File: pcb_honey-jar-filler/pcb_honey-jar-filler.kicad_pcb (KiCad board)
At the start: 2 copper layers, 160 x 100 mm, 88 parts, among them J1 12V, 5V, J10 OLED_3v3, GND, J11 OLED_SDA, SCL, J12 MOS out (COM, Drain), J13 230V Heater, J14 3V3, J15 12V, 5V, J16 LED2, J17 GND, J18 GND, J19 Servo, J2 12V, J20 Conn_01x07_Pin, J21 LED1, J22 Reserve, J23 Relay fallback, J24 load-cell (red, black), J25 load-cell (white, green), J26 B+ B- (free), J27 Supply, J3 3V3, J4 button1, button2, J5 4...7V, J6 Encoder A, B, J7 Encoder Button, Pos-sw, J8 MOS out (COM, Drain), K1 RT314A24, K4 RT314A24, K5 RT314A24, M1 DC-worm-gear motor (Carousell), Q1 IRLB8721PBF, Q2 IRLB8721PBF, U1 esp32-devkit-v1_30Pin, U10 LM2576T-ADJ, U3 ULN2003, U4 HX711_24-bit-ADC_weight-scale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, U9 LM2576T-5

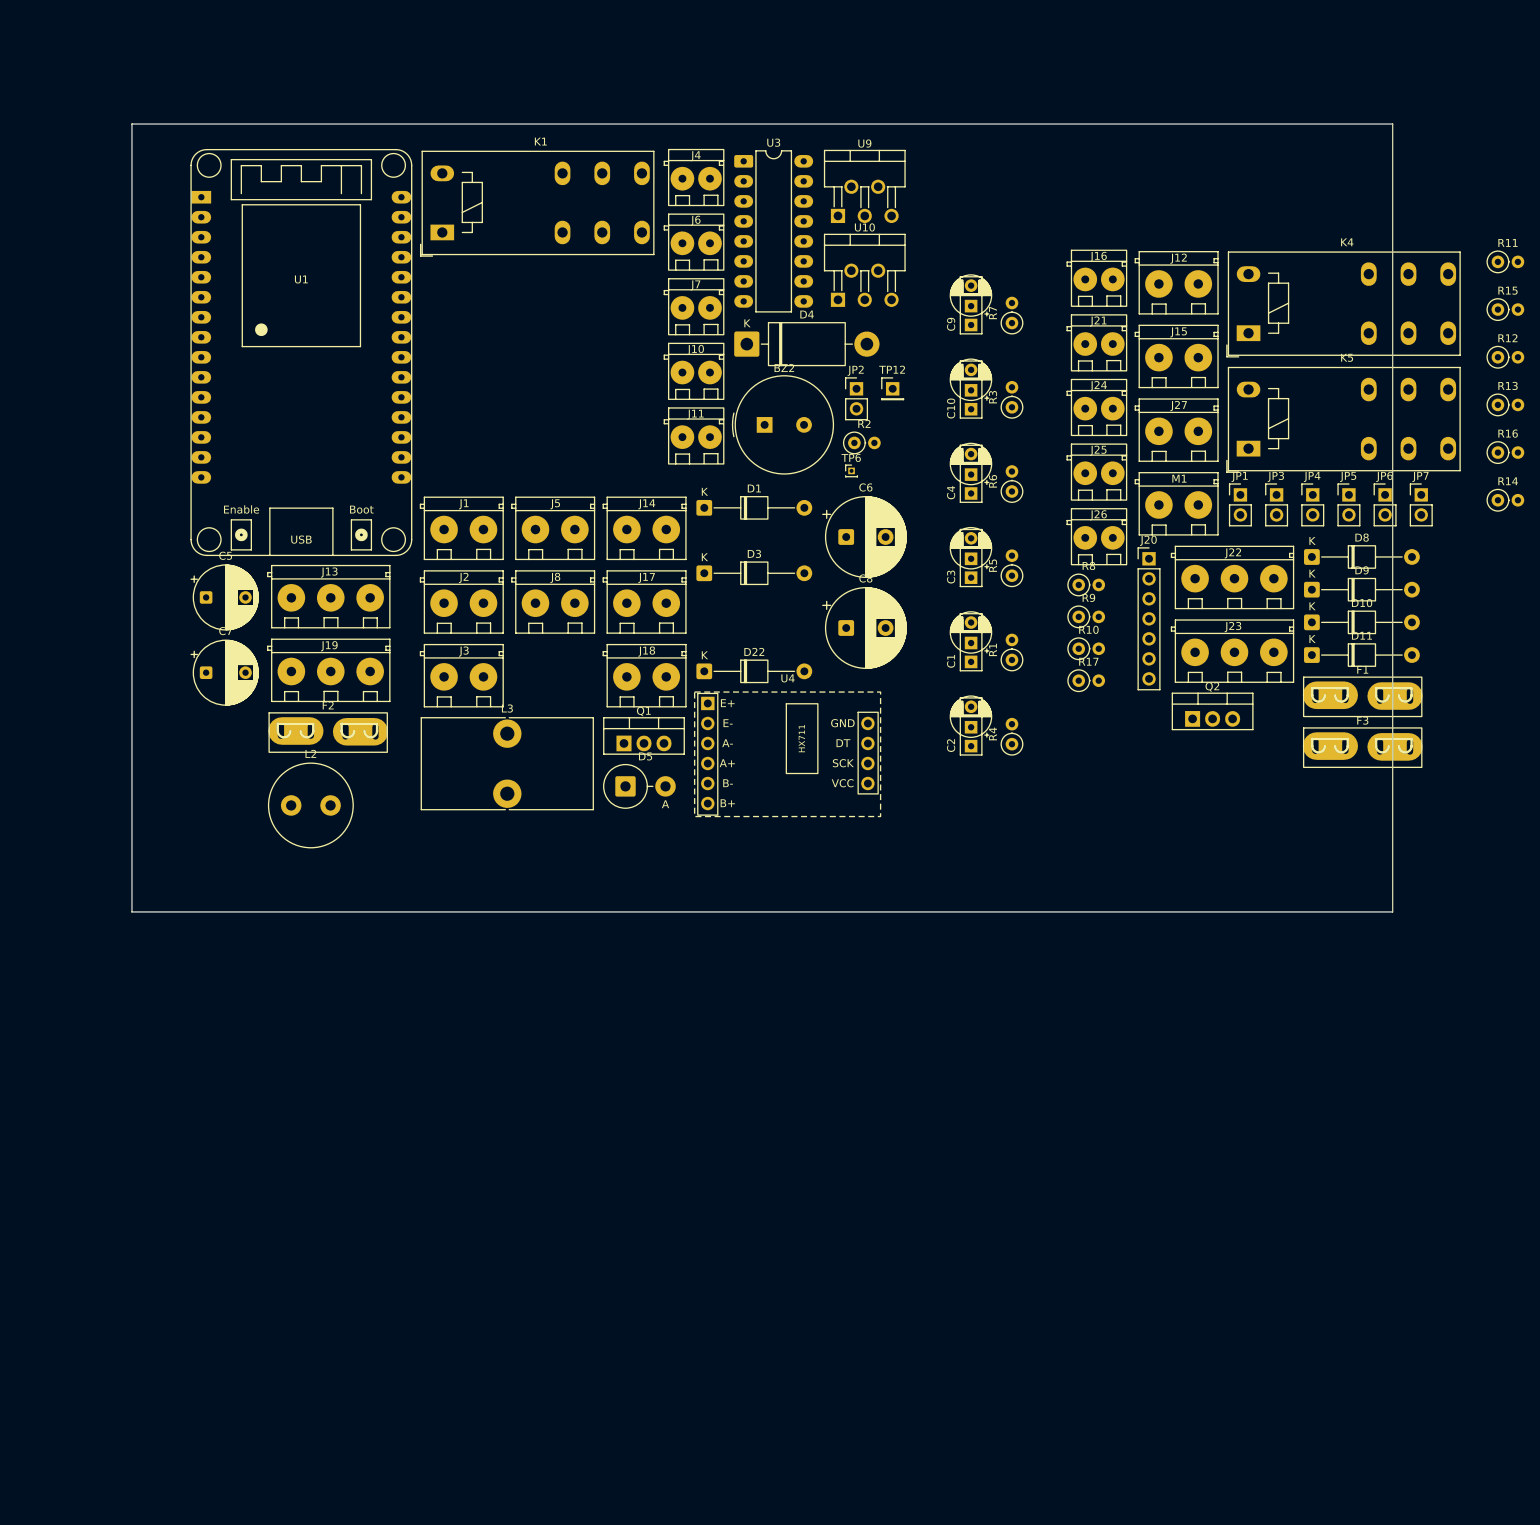
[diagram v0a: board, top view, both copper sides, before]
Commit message: pcb: arrange parts, re-assign, add servo-cutoff
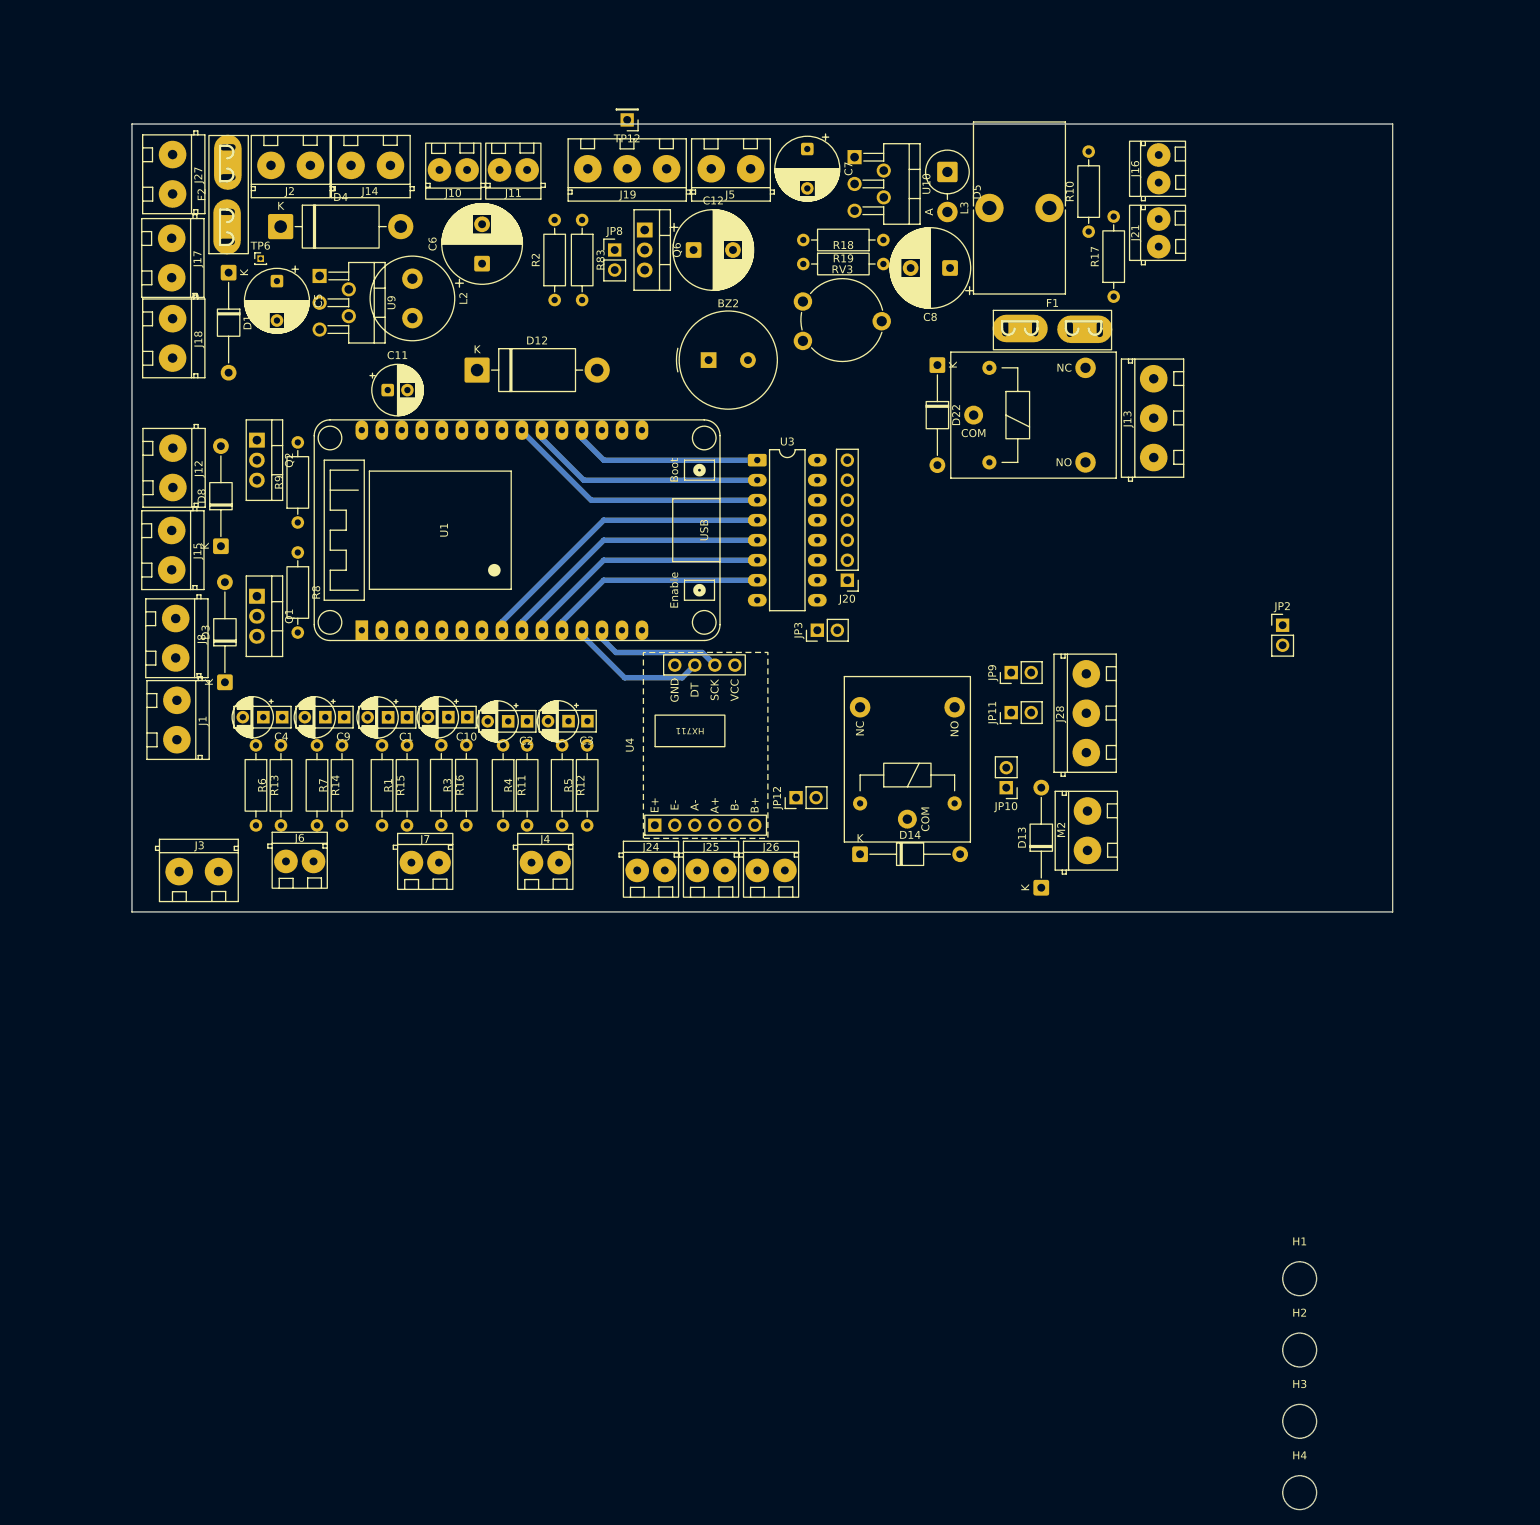
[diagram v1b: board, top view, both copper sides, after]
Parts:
- removed D10, D11, D9: D, Diode_THT:D_T-1_P12.70mm_Horizontal
- removed F3: F-Heater, misc_libJonny:Fuseholder_Automotive-Mini_Fuse11x4x16_Footprint15x5_Inline
- removed J22: Reserve, terminals_libJonny:ScrewTerminal_P5mm_3Pin_FP15x8
- removed J23: Relay fallback, terminals_libJonny:ScrewTerminal_P5mm_3Pin_FP15x8
- removed JP1, JP4, JP5, JP6, JP7: Jumper_2_Bridged, Connector_PinHeader_2.54mm:PinHeader_1x02_P2.54mm_Vertical
- removed K1, K4, K5: RT314A24, Relay_THT:Relay_SPDT_Schrack-RT1-16A-FormC_RM5mm
- removed M1: DC-worm-gear motor (Carousell), terminals_libJonny:ScrewTerminal_P5mm_2Pin_FP10x8
- added C11: 15u, Capacitor_THT:CP_Radial_D6.3mm_P2.50mm, F.Cu at (52.2, 52.1)
- added C12: 2200uF, Capacitor_THT:CP_Radial_D10.0mm_P5.00mm, F.Cu at (91.0, 34.3)
- added D12: 1N5822, Diode_THT:D_DO-201AD_P15.24mm_Horizontal, F.Cu at (63.5, 49.5)
- added D13: D, Diode_THT:D_T-1_P12.70mm_Horizontal, F.Cu at (135.1, 115.2)
- added D14: D, Diode_THT:D_T-1_P12.70mm_Horizontal, F.Cu at (112.1, 111.0)
- added H1: MountingHole, MountingHole:MountingHole_4.3mm_M4_DIN965, F.Cu at (167.9, 164.8)
- added H2: MountingHole, MountingHole:MountingHole_4.3mm_M4_DIN965, F.Cu at (167.9, 173.9)
- added H3: MountingHole, MountingHole:MountingHole_4.3mm_M4_DIN965, F.Cu at (167.9, 182.9)
- added H4: MountingHole, MountingHole:MountingHole_4.3mm_M4_DIN965, F.Cu at (167.9, 192.0)
- added J28: Relay fallback, terminals_libJonny:ScrewTerminal_P5mm_3Pin_FP15x8, F.Cu at (140.8, 98.1)
- added JP10: Jumper_2_Bridged, Connector_PinHeader_2.54mm:PinHeader_1x02_P2.54mm_Vertical, F.Cu at (130.7, 102.5)
- added JP11: Jumper_2_Bridged, Connector_PinHeader_2.54mm:PinHeader_1x02_P2.54mm_Vertical, F.Cu at (131.3, 93.0)
- added JP12: Jumper_2_Bridged, Connector_PinHeader_2.54mm:PinHeader_1x02_P2.54mm_Vertical, F.Cu at (104.0, 103.8)
- added JP8: Force-on-servo, Connector_PinHeader_2.54mm:PinHeader_1x02_P2.54mm_Vertical, F.Cu at (81.0, 34.3)
- added JP9: Jumper_2_Bridged, Connector_PinHeader_2.54mm:PinHeader_1x02_P2.54mm_Vertical, F.Cu at (131.3, 87.9)
- added K6: Relay_LEG-xxF, relays_libJonny:Relay_LEG-xxF, F.Cu at (134.6, 55.2)
- added K7: Relay_LEG-xxF, relays_libJonny:Relay_LEG-xxF, F.Cu at (118.1, 98.4)
- added M2: DC-worm-gear motor (Carousell), terminals_libJonny:ScrewTerminal_P5mm_2Pin_FP10x8, F.Cu at (141.0, 110.5)
- added Q6: IRF5305, Package_TO_SOT_THT:TO-220-3_Vertical, F.Cu at (84.8, 31.8)
- added R18: 5k6, Resistor_THT:R_Axial_DIN0207_L6.3mm_D2.5mm_P10.16mm_Horizontal, F.Cu at (104.9, 36.1)
- added R19: 2k2, Resistor_THT:R_Axial_DIN0207_L6.3mm_D2.5mm_P10.16mm_Horizontal, F.Cu at (115.1, 33.0)
- added R83: 47k, Resistor_THT:R_Axial_DIN0207_L6.3mm_D2.5mm_P10.16mm_Horizontal, F.Cu at (76.8, 30.5)
- added RV3: 10k, resistors_libJonny:Potentiometer_Piher_PT-10-V10_Vertical, F.Cu at (104.9, 45.8)
- L3: value 470u -> 100u
- R1, R10, R11, R12, R13, R14, R15, R16, R17, R2, R3, R4, R5, R6, R7, R8, R9: footprint Resistor_THT:R_Axial_DIN0207_L6.3mm_D2.5mm_P2.54mm_Vertical -> Resistor_THT:R_Axial_DIN0207_L6.3mm_D2.5mm_P10.16mm_Horizontal
- moved R13 163.4 mm to (35.4, 97.2), turned to -90 degrees
- moved R14 153.1 mm to (43.2, 97.2), turned to -90 degrees
- moved R15 152.0 mm to (51.4, 97.2), turned to -90 degrees
- moved R11 140.4 mm to (66.8, 97.2), turned to -90 degrees
- moved R16 139.1 mm to (59.0, 97.1), turned to -90 degrees
- moved D8 138.5 mm to (31.0, 71.9), turned to 90 degrees
- moved J27 130.0 mm to (24.9, 22.2), turned to -90 degrees
- moved R12 128.6 mm to (74.3, 97.2), turned to -90 degrees
- moved J15 127.2 mm to (24.7, 69.9), turned to -90 degrees
- moved J12 126.9 mm to (24.9, 59.4), turned to -90 degrees
- moved Q2 123.9 mm to (35.6, 58.4), turned to -90 degrees
- moved J13 110.9 mm to (149.4, 60.6), turned to 90 degrees
- moved R7 106.3 mm to (46.4, 107.3)
- moved R6 102.0 mm to (38.6, 107.3)
- moved C7 101.2 mm to (105.4, 21.5), turned to -90 degrees
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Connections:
- F1 pad 2: Net-(J13-Pin_3) -> Net-(J13-Pin_2)
- J19 pad 1: 4...7V -> Net-(J19-Pin_1)
- J20 pad 1: /FREE -> /OD_Relay-reserve
- J20 pad 2: /OD_Relay-heater -> /OD_Relay-motor
- J20 pad 3: /OD_Relay-motor -> /OD_Relay-heater
- J20 pad 4: /OD_Relay-reserve -> /OD_LED1
- J20 pad 5: /OD_LED1 -> /OD_LED2
- J20 pad 6: /OD_LED2 -> /OD_Buzzer
- J20 pad 7: /OD_Buzzer -> /OD_EN-Servo-pwr
- U1 pad 1: unconnected-(U1-EN-Pad1) -> Net-(U1-EN)
- U1 pad 10: unconnected-(U1-GPIO27/ADC2-Pad10) -> /GPIO_Relay-motor
- U1 pad 11: unconnected-(U1-GPIO14/ADC2/HSPI_CLK-Pad11) -> /GPIO_Relay-reserve
- U1 pad 12: unconnected-(U1-GPIO12/HSPI-MISO/MTDI/[LOW-AT-BOOT]-Pad12) -> /HX711_DT
- U1 pad 13: unconnected-(U1-GPIO13/HSPI-MOSI-Pad13) -> /HX711_SCK
- U1 pad 14: unconnected-(U1-GND-Pad14) -> GND
- U1 pad 15: +5V -> Net-(D12-K)
- U1 pad 17: unconnected-(U1-GND-Pad17) -> GND
- U1 pad 19: unconnected-(U1-GPIO2/ADC2/[OnboardBlueLED+10k_down]-Pad19) -> /GPIO_EN-Servo-pwr
- U1 pad 2: unconnected-(U1-GPIO36/ADC1-CH0/SENSOR_VP/[IN-ONLY]-Pad2) -> /GPIO-IN_Encoder-A
- U1 pad 20: unconnected-(U1-GPIO4/ADC2-Pad20) -> /Servo-PWM-Signal
- U1 pad 21: unconnected-(U1-GPIO16/UART2-RX-Pad21) -> /GPIO_Buzzer
- U1 pad 22: unconnected-(U1-GPIO17/UART2-TX-Pad22) -> /GPIO_LED2
- U1 pad 23: unconnected-(U1-GPIO5/VSPI-CS-Pad23) -> /GPIO_MOS-reserve
- U1 pad 24: unconnected-(U1-GPIO18/VSPI_CLK-Pad24) -> /GPIO_MOS-valve
- U1 pad 26: unconnected-(U1-GPIO21/I2C-SDA-Pad26) -> /I2C-SDA_OLED
- U1 pad 29: unconnected-(U1-GPIO22/I2C-SCL-Pad29) -> /I2C-SCL_OLED
- U1 pad 3: unconnected-(U1-GPIO39/ADC1-CH3/SENSOR_VN/[IN-ONLY]-Pad3) -> /GPIO-IN_Encoder-B
- U1 pad 4: unconnected-(U1-GPIO34/ADC1-CH6//[IN-ONLY]-Pad4) -> /GPIO-IN_Encoder-Button
- U1 pad 5: unconnected-(U1-GPIO35/ADC1-CH7/[IN-ONLY]-Pad5) -> /GPIO-IN_Position-SW
- U1 pad 6: unconnected-(U1-GPIO32/ADC1-CH4-Pad6) -> /GPIO-IN_Button1
- U1 pad 7: unconnected-(U1-GPIO33/ADC1-CH5-Pad7) -> /GPIO-IN_Button2
- U1 pad 8: unconnected-(U1-GPIO25/ADC2-Pad8) -> /GPIO_LED1
- U1 pad 9: unconnected-(U1-GPIO26/ADC2-Pad9) -> /GPIO_Relay-heater
- U10 pad 4: 4...7V -> Net-(U10-FB)
- U3 pad 1: /GPIO_Buzzer -> /GPIO_EN-Servo-pwr
- U3 pad 10: /FREE -> /OD_Relay-reserve
- U3 pad 11: /OD_Relay-heater -> /OD_Relay-motor
- U3 pad 12: /OD_Relay-motor -> /OD_Relay-heater
- U3 pad 13: /OD_Relay-reserve -> /OD_LED1
- U3 pad 14: /OD_LED1 -> /OD_LED2
- U3 pad 15: /OD_LED2 -> /OD_Buzzer
- U3 pad 16: /OD_Buzzer -> /OD_EN-Servo-pwr
- U3 pad 2: /GPIO_LED2 -> /GPIO_Buzzer
- U3 pad 3: /GPIO_LED1 -> /GPIO_LED2
- U3 pad 4: /GPIO_Relay-reserve -> /GPIO_LED1
- U3 pad 5: /GPIO_Relay-motor -> /GPIO_Relay-heater
- U3 pad 6: /GPIO_Relay-heater -> /GPIO_Relay-motor
- U3 pad 7: unconnected-(U3-I7-Pad7) -> /GPIO_Relay-reserve
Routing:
- net /GPIO_LED1: track 0.00 -> 38.8 mm
- net /GPIO_Relay-heater: track 0.00 -> 35.2 mm
- net /GPIO_LED2: track 0.00 -> 33.6 mm
- net /GPIO_Relay-motor: track 0.00 -> 31.6 mm
- net /GPIO_Buzzer: track 0.00 -> 30.6 mm
- net /GPIO_Relay-reserve: track 0.00 -> 28.0 mm
- net /GPIO_EN-Servo-pwr: track 0.00 -> 24.4 mm
- net /HX711_DT: track 0.00 -> 17.8 mm
- net /HX711_SCK: track 0.00 -> 16.8 mm
